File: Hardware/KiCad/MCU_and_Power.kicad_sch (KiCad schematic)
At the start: 62 parts

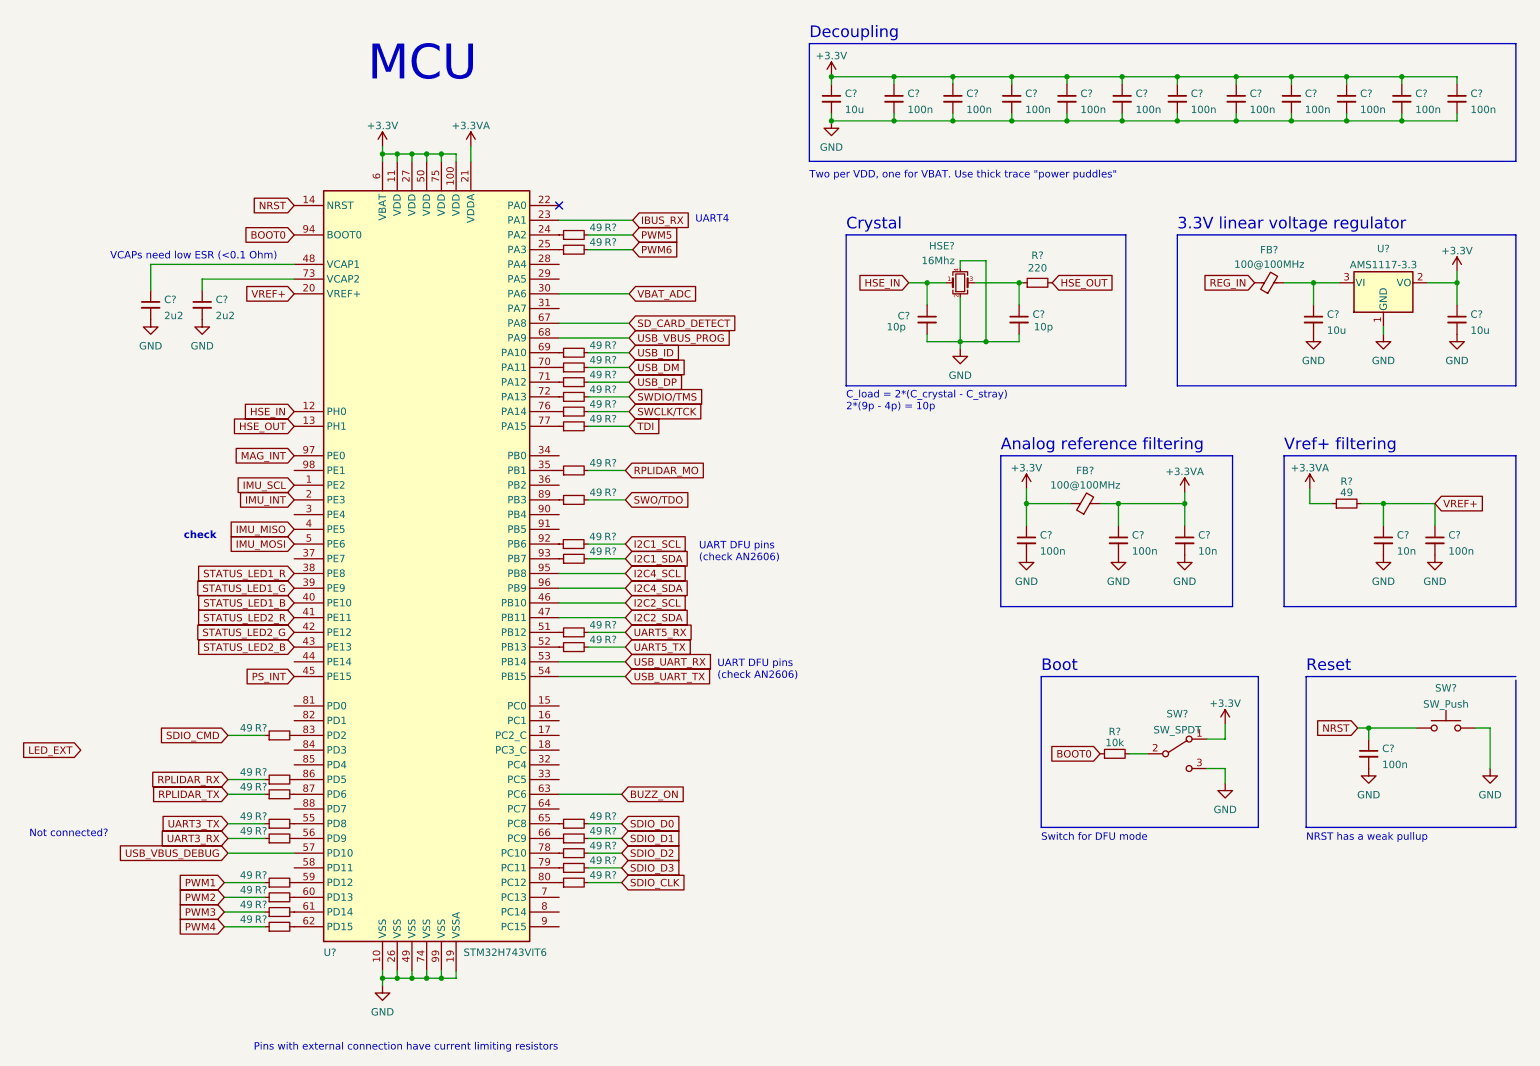
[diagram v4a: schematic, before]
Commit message: Added a missing connection between the BECs and the LDO, removed some duplicate ferrite bead filtering
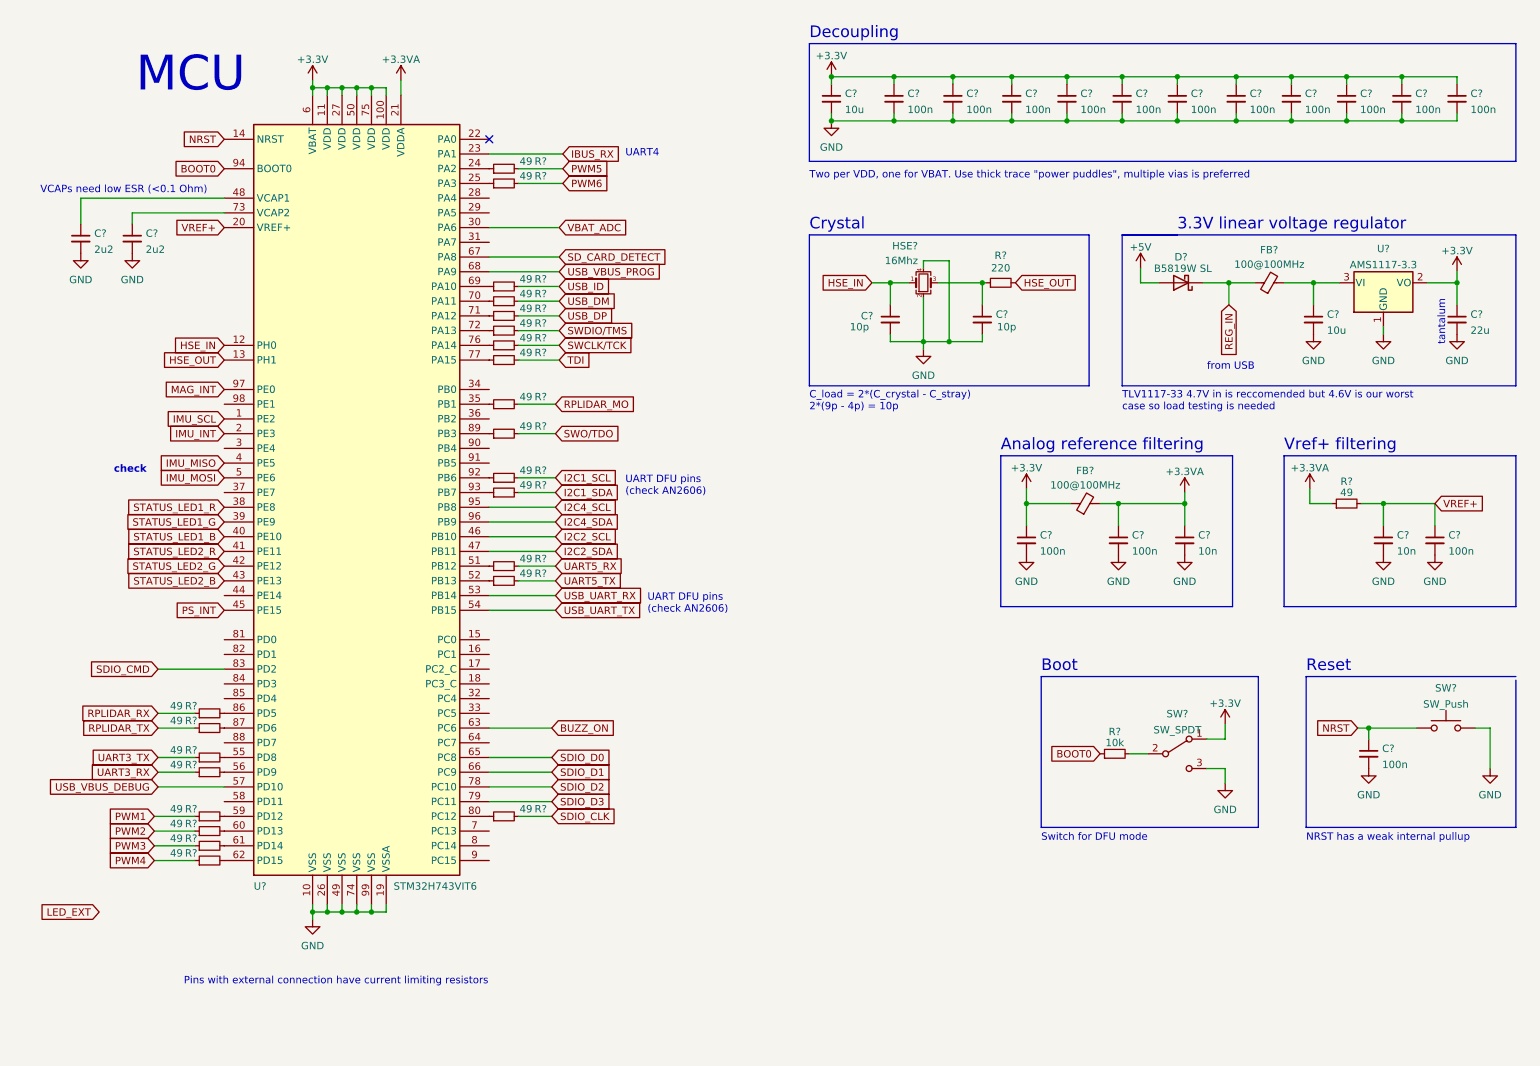
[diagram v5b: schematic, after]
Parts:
- removed R? (x5): 49, Resistor_SMD:R_0402_1005Metric, symbol Device:R_Small
- added D?: B5819W SL, Diode_SMD:D_SOD-123, symbol flightController:B5819W SL
- C?: value 10u -> 22u
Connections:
- net REG_IN: now also D?.1 (K)
- net SDIO_CMD: now also U?.83 (PD2)
- net SDIO_D0: now also U?.65 (PC8)
- net SDIO_D1: now also U?.66 (PC9)
- net SDIO_D2: now also U?.78 (PC10)
- net SDIO_D3: now also U?.79 (PC11)
- net at U?.92 (PB6): now also R?.1
- new net +5V: D?.2 (A)
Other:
- note added: "NRST has a weak internal pullup"
- note added: "TLV1117-33 4.7V in is reccomended but 4.6V is our worst case so load testing is needed"
- note added: "Two per VDD, one for VBAT. Use thick trace "power puddles", multiple vias is preferred"
- note added: "from USB"
- note added: "tantalum"
- note removed: "NRST has a weak pullup"
- note removed: "Not connected?"
- note removed: "Two per VDD, one for VBAT. Use thick trace "power puddles""
- moved on the sheet: C?, HSE?, R?, U?

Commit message: Added more filtering for the BMP, small labeling changes
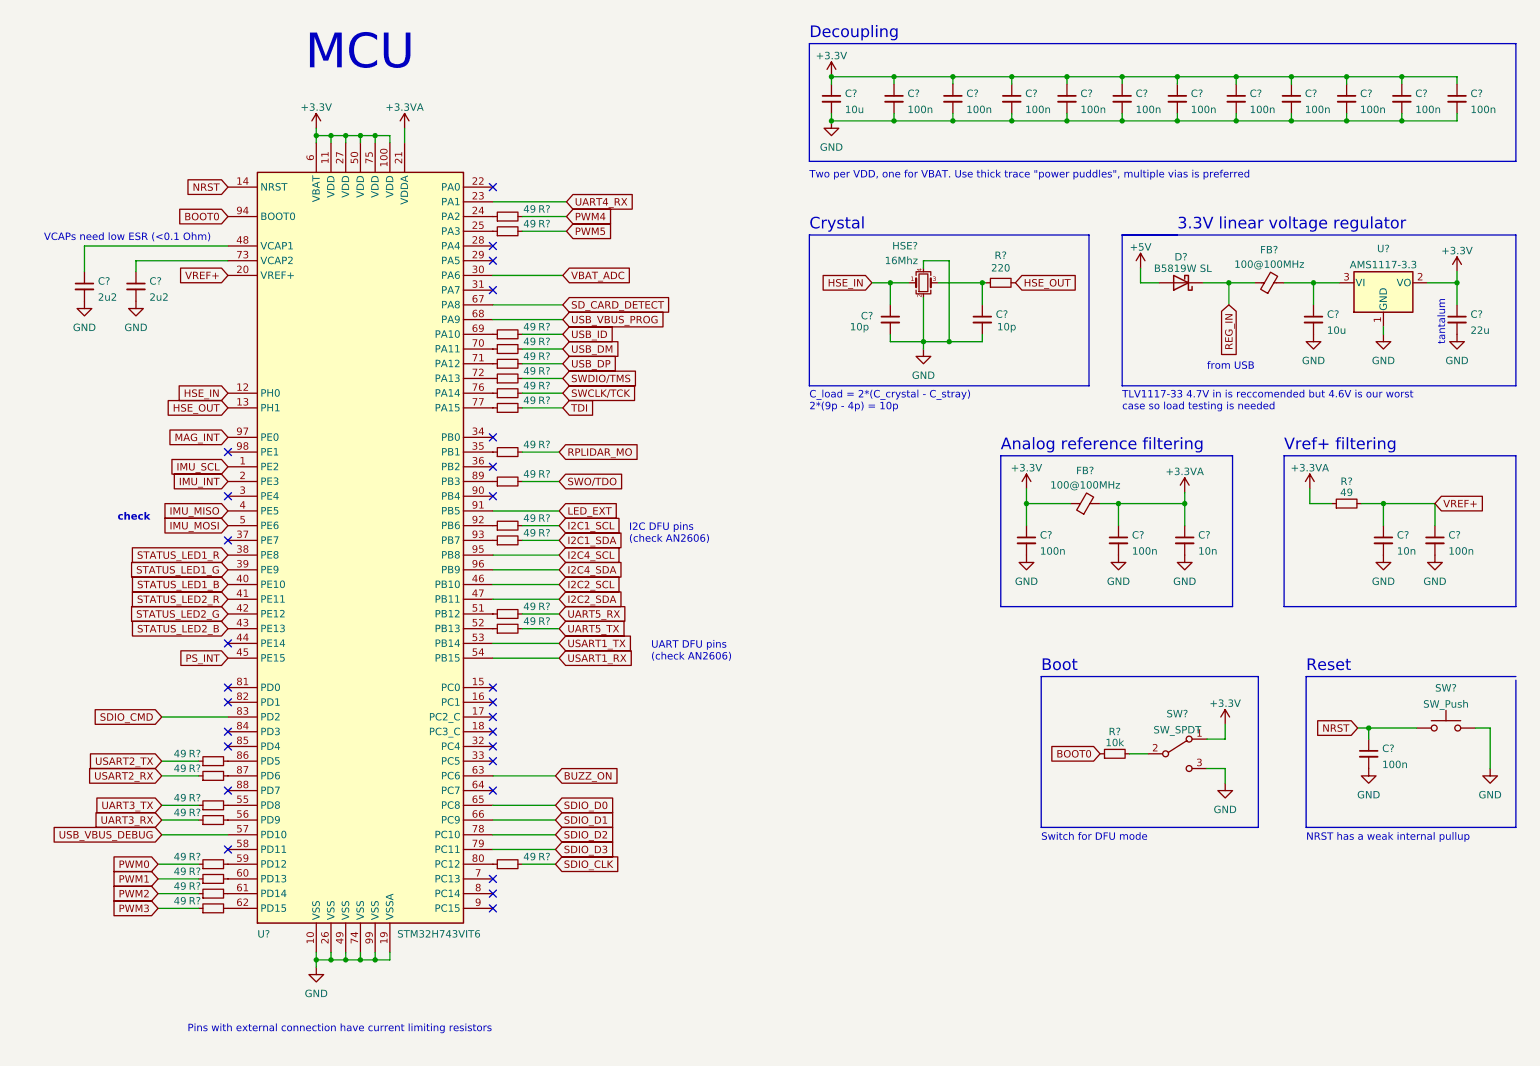
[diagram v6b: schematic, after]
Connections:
- net PWM6 is gone; now on net PWM5: R?.2
- net LED_EXT: now also U?.91 (PB5)
- net PWM1: now also R?.1; no longer R?.1
- net PWM2: now also R?.1; no longer R?.1
- net PWM3: now also R?.1; no longer R?.1
- net PWM4: now also R?.2; no longer R?.1
- net PWM5: no longer R?.2
- net IBUS_RX renamed UART4_RX
- net RPLIDAR_RX renamed USART2_TX
- net RPLIDAR_TX renamed USART2_RX
- net USB_UART_RX renamed USART1_TX
- net USB_UART_TX renamed USART1_RX
- new net PWM0: R?.1
- no-connect marks 1 -> 27
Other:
- note added: "I2C DFU pins (check AN2606)"
- note removed: "UART4"
- moved on the sheet: C?, R?, U?

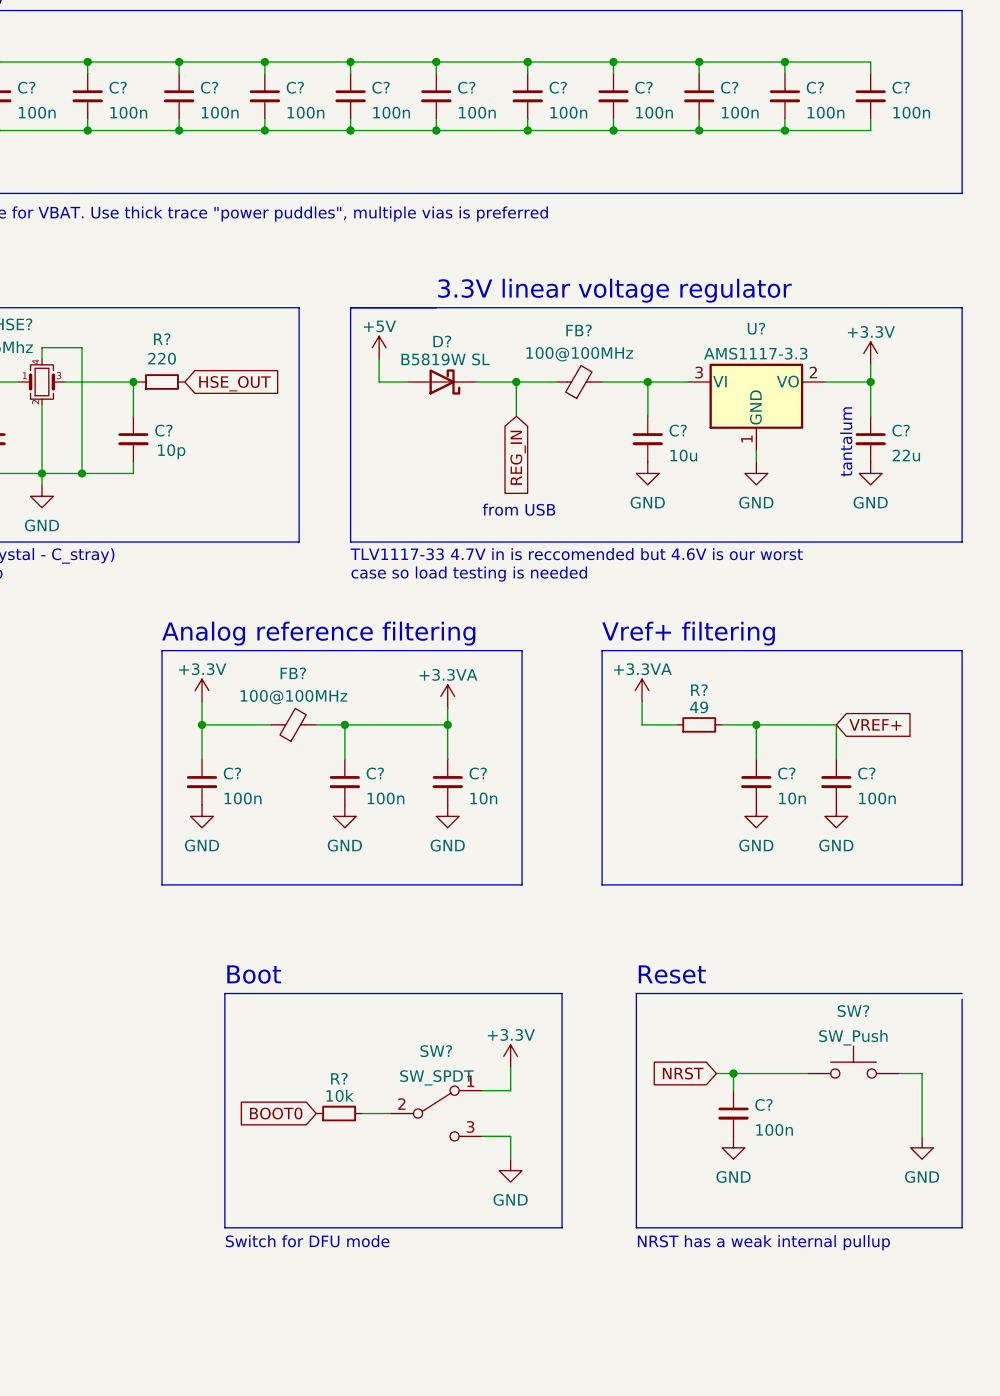
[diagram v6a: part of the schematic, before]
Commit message: Fixed duplicate external LED driver
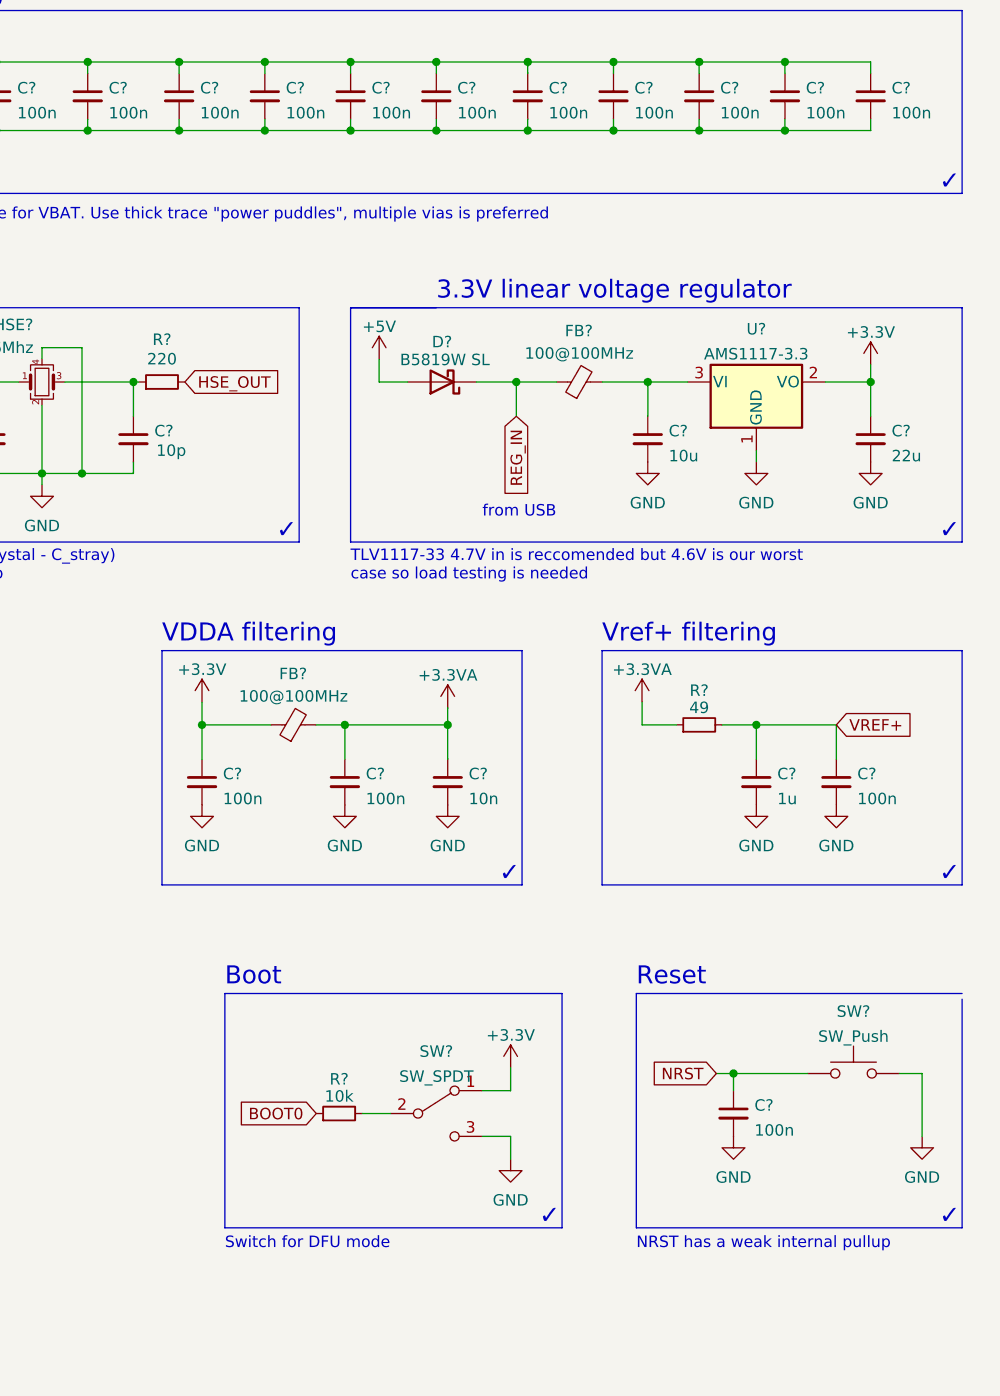
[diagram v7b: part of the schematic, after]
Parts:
- removed C?: 10n, Capacitor_SMD:C_0402_1005Metric, symbol Device:C_Small
- added C?: 1u, Capacitor_SMD:C_0603_1608Metric, symbol Device:C_Small
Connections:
- net GND: now also C?.2
- net VREF+: now also C?.1
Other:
- note added: "VDDA filtering"
- note added: "✓"
- note removed: "Analog reference filtering"
- note removed: "tantalum"
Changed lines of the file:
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@@
+    (effects (font (size 2 2)) (justify left bottom))
+  )
+  (text "✓" (at 222.885 119.38 0)
     (effects (font (size 2 2)) (justify left bottom))
   )
@@
     (effects (font (size 1.27 1.27) (thickness 0.254) bold) (justify left bottom))
   )
+  (text "✓" (at 271.78 42.545 0)
+    (effects (font (size 2 2)) (justify left bottom))
+  )
+  (text "✓" (at 198.12 81.28 0)
+    (effects (font (size 2 2)) (justify left bottom))
+  )
   (text "3.3V linear voltage regulator" (at 215.9 54.61 0)
     (effects (font (size 2 2)) (justify left bottom))
@@
     (effects (font (size 1.27 1.27)) (justify left bottom))
   )
-  (text "Analog reference filtering" (at 185.42 92.71 0)
+  (text "VDDA filtering" (at 185.42 92.71 0)
     (effects (font (size 2 2)) (justify left bottom))
   )
@@
     (effects (font (size 2 2)) (justify left bottom))
   )
-  (text "tantalum" (at 262.255 74.295 90)
-    (effects (font (size 1.27 1.27)) (justify left bottom))
-  )
   (text "NRST has a weak internal pullup" (at 238.125 160.02 0)
     (effects (font (size 1.27 1.27)) (justify left bottom))
   )
   (text "Crystal" (at 152.4 54.61 0)
+    (effects (font (size 2 2)) (justify left bottom))
+  )
+  (text "✓" (at 271.78 157.48 0)
+    (effects (font (size 2 2)) (justify left bottom))
+  )
+  (text "✓" (at 227.33 157.48 0)
     (effects (font (size 2 2)) (justify left bottom))
   )
@@
     (effects (font (size 1.27 1.27)) (justify left bottom))
   )
+  (text "✓" (at 271.78 119.38 0)
+    (effects (font (size 2 2)) (justify left bottom))
+  )
   (text "I2C DFU pins \n(check AN2606)" (at 121.285 108.585 0)
     (effects (font (size 1.27 1.27)) (justify left bottom))
@@
   (text "Switch for DFU mode" (at 192.405 160.02 0)
     (effects (font (size 1.27 1.27)) (justify left bottom))
+  )
+  (text "✓" (at 271.78 81.28 0)
+    (effects (font (size 2 2)) (justify left bottom))
   )
   (text "C_load = 2*(C_crystal - C_stray) \n2*(9p - 4p) = 10p"
@@
     (pin "99")
   )
-  (symbol (lib_id "Device:C_Small") (at 251.46 107.95 0) (unit 1)
-    (in_bom yes) (on_board yes) (fields_autoplaced)
-    (property "Reference" "C?" (id 0) (at 253.7841 107.0478 0)
-      (effects (font (size 1.27 1.27)) (justify left))
-    )
-    (property "Value" "10n" (id 1) (at 253.7841 109.8229 0)
-      (effects (font (size 1.27 1.27)) (justify left))
-    )
-    (property "Footprint" "Capacitor_SMD:C_0402_1005Metric" (id 2) (at 251.46 107.95 0)
-      (effects (font (size 1.27 1.27)) hide)
-    )
-    (property "Datasheet" "~" (id 3) (at 251.46 107.95 0)
-      (effects (font (size 1.27 1.27)) hide)
-    )
-    (pin "1")
-    (pin "2")
-  )
   (symbol (lib_id "power:+3.3VA") (at 217.17 99.695 0) (unit 1)
     (in_bom yes) (on_board yes) (fields_autoplaced)
@@
     (pin "1")
   )
+  (symbol (lib_id "Device:C_Small") (at 251.46 107.95 0) (unit 1)
+    (in_bom yes) (on_board yes) (fields_autoplaced)
+    (property "Reference" "C?" (id 0) (at 253.7841 107.0478 0)
+      (effects (font (size 1.27 1.27)) (justify left))
+    )
+    (property "Value" "1u" (id 1) (at 253.7841 109.8229 0)
+      (effects (font (size 1.27 1.27)) (justify left))
+    )
+    (property "Footprint" "Capacitor_SMD:C_0603_1608Metric" (id 2) (at 251.46 107.95 0)
+      (effects (font (size 1.27 1.27)) hide)
+    )
+    (property "Datasheet" "~" (id 3) (at 251.46 107.95 0)
+      (effects (font (size 1.27 1.27)) hide)
+    )
+    (pin "1")
+    (pin "2")
+  )
   (symbol (lib_id "Device:C_Small") (at 245.11 31.75 0) (unit 1)
